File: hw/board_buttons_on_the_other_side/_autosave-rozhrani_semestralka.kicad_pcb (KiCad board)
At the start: 2 copper layers, 152 x 38.6 mm, 64 parts, among them P1 DISPLAY_CONN, P2 DISPLAY_VCC_CON, P3 USB_B, U1 MCP2210, U2 MIC5504-3.3, U3 Joystick, U4 LM239, U5 CD4532, U6 NPIC6C596, U7 NE555, U8 PB6149L, U9 PB6149L

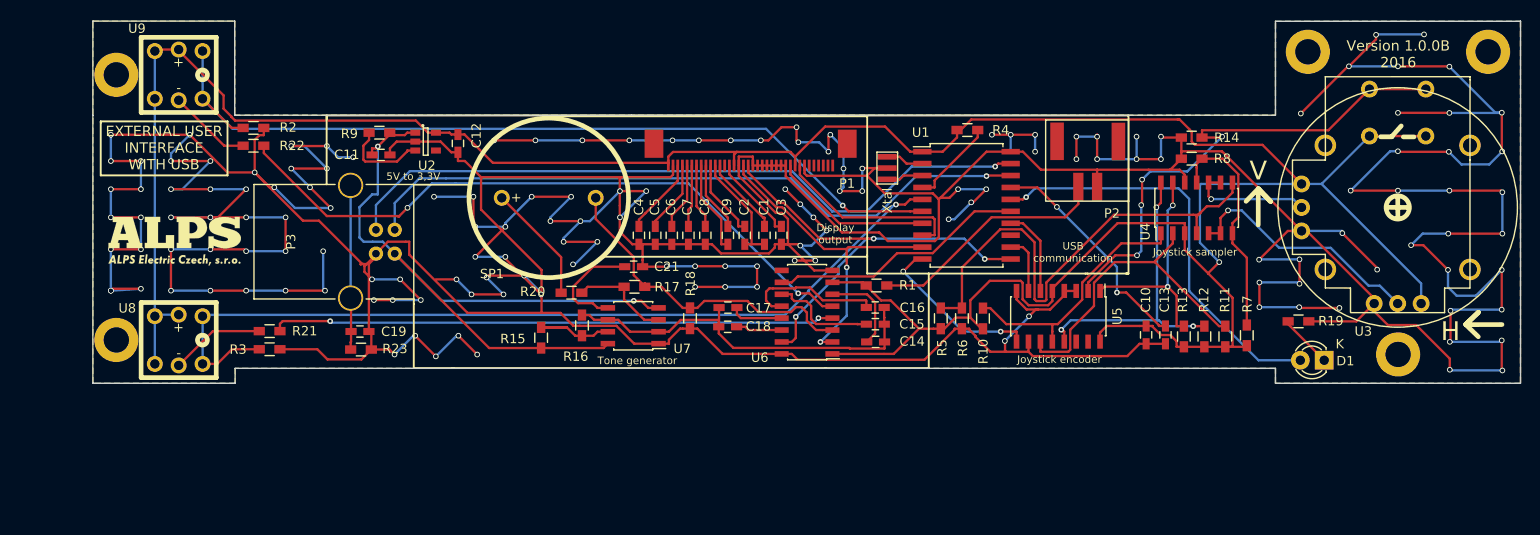
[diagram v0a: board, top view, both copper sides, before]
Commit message: Aladin v 1.2.0 pcb - repaired GPIO for /CE and also BUZZERs capacitors, some footprints had change
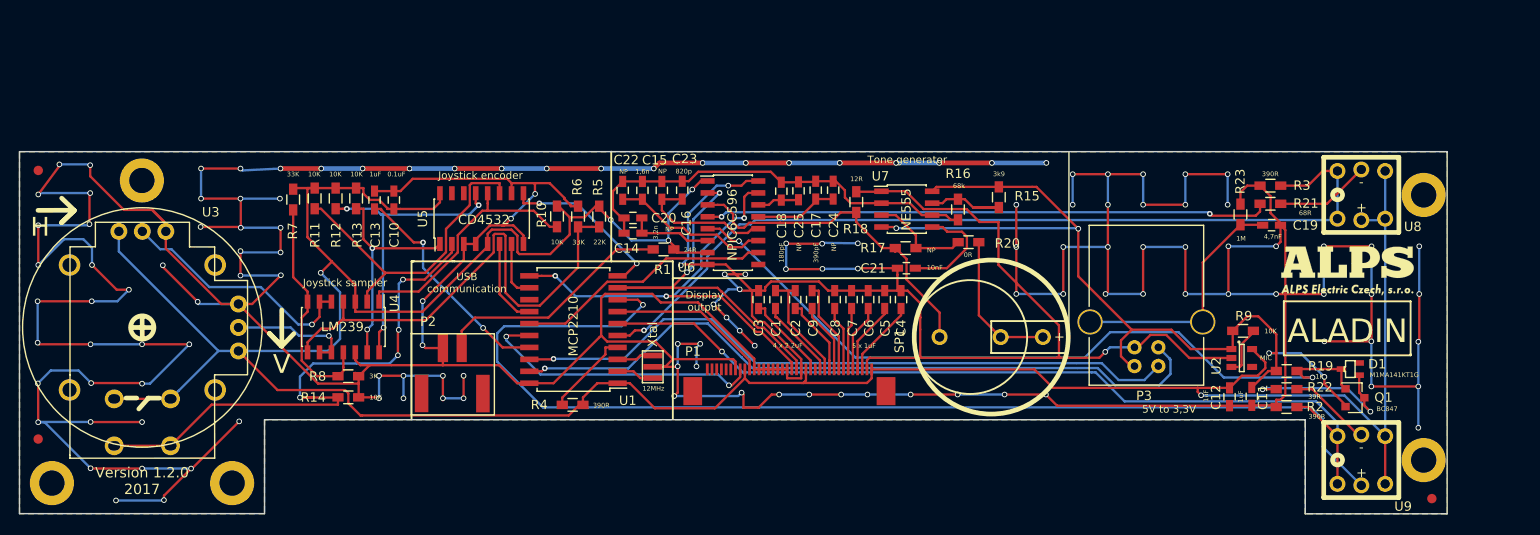
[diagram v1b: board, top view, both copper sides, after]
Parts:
- added C20: NP, Capacitors_SMD:C_0603_HandSoldering, F.Cu at (132.2, 103.7)
- added C22: NP, Capacitors_SMD:C_0603_HandSoldering, F.Cu at (131.1, 100.7)
- added C23: NP, Capacitors_SMD:C_0603_HandSoldering, F.Cu at (135.3, 100.7)
- added C24: NP, Capacitors_SMD:C_0603_HandSoldering, F.Cu at (153.5, 100.7)
- added C25: NP, Capacitors_SMD:C_0603_HandSoldering, F.Cu at (149.8, 100.8)
- added FID1: Fiducial_1mm_Dia_2.54mm_Outer_CopperTop, Fiducials:Fiducial_1mm_Dia_2.54mm_Outer_CopperTop, F.Cu at (68.9, 98.6)
- added FID2: Fiducial_1mm_Dia_2.54mm_Outer_CopperTop, Fiducials:Fiducial_1mm_Dia_2.54mm_Outer_CopperTop, F.Cu at (68.9, 127.2)
- added FID3**: Fiducial_1mm_Dia_2.54mm_Outer_CopperTop, Fiducials:Fiducial_1mm_Dia_2.54mm_Outer_CopperTop, F.Cu at (217.2, 133.5)
- added Q1: BC847, TO_SOT_Packages_SMD:SOT-23, F.Cu at (209.1, 122.8)
- C14: value 0 -> 3,2n
- C15: value 0 -> 1,6n
- C16: value 0 -> 820p
- C17: value 0 -> 390pF
- C18: value 0 -> 180pF
- D1: value L-1334SRT -> M1MA141KT1G; footprint LEDs:LED-3MM -> TO_SOT_Packages_SMD:SOT-323
- R1: value 24 -> 24R
- R17: value 10K -> NP
- R18: value 10K -> 12R
- R19: value 390R -> 1K
- R2, R3, R4: value 390 -> 390R
- R21: value 68 -> 68R
- R22: value 68 -> 39R
- U2: value MIC5504-3.3 -> MIC
- U9: value PB6149L -> PB6149Ldual
- moved REF** 159.7 mm to (70.3, 131.9), turned to 180 degrees
- moved REF** 145.1 mm to (216.4, 129.4), turned to 180 degrees
- moved REF** 140.0 mm to (216.4, 101.2), turned to 180 degrees
- moved REF** 135.0 mm to (79.9, 99.7), turned to 180 degrees
- moved U3 134.3 mm to (80.0, 115.3), turned to 180 degrees
- moved U9 132.4 mm to (209.7, 129.4), turned to 180 degrees
- moved U8 126.9 mm to (209.7, 101.2), turned to 180 degrees
- moved G*** 124.9 mm to (208.3, 109.3)
- moved REF** 123.4 mm to (89.5, 131.9), turned to 180 degrees
- moved R2 113.9 mm to (201.8, 123.8), turned to 0 degrees
- moved R22 113.0 mm to (201.8, 121.9), turned to 0 degrees
- moved R3 108.0 mm to (200.1, 100.2), turned to 180 degrees
- moved R21 107.4 mm to (200.1, 102.2), turned to 180 degrees
- moved R7 102.6 mm to (96.0, 101.7), turned to 90 degrees
- moved R11 98.1 mm to (98.3, 101.6), turned to 90 degrees
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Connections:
- D1 pad 1: Net-(D1-Pad1) -> /BUT_LED
- D1 pad 2: /SIGNAL_LED -> Net-(D1-Pad2)
- R19 pad 1: GND -> /REG2
- R19 pad 2: Net-(D1-Pad1) -> VCC
- R22 pad 1: /REG2 -> /BUT_LED
- U1 pad 16: /SIGNAL_LED -> //CE
- U1 pad 8: //CE -> /SIGNAL_LED
- U9 pad 3: +3V3 -> /SIGNAL_LED
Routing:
- net /SIGNAL_LED: track 44.7 -> 122.0 mm
- net GND: track 966.4 -> 944.1 mm, vias 153 -> 137
- net /BUT_LED: track 0.00 -> 18.4 mm, vias 0 -> 2
- net VCC: track 79.1 -> 95.7 mm, vias 2 -> 4
- net //CE: track 20.3 -> 31.6 mm, vias 0 -> 2
- net /REG2: track 71.1 -> 82.2 mm
- net Net-(C19-Pad1): track 17.5 -> 26.4 mm
- net (no net): track 8.20 -> 0.00 mm, vias 4 -> 0
- net /MOSI: track 35.7 -> 42.5 mm
- net /JOY_C: track 54.6 -> 61.3 mm
- net Net-(D1-Pad1): track 6.30 -> 0.00 mm
- net +3V3: track 325.5 -> 331.8 mm, vias 1 -> 5
- net /REG4: track 11.4 -> 16.9 mm
- net Net-(R9-Pad2): track 9.27 -> 5.34 mm
- net Net-(C14-Pad1): track 42.0 -> 45.4 mm
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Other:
- outline, holes or cut-outs redrawn
- board text added: "4 x 2.2uF"
- board text added: "5 x 1uF"
- board text added: "ALADIN"
- board text added: "Version 1.2.0 2017"
- board text removed: "EXTERNAL USER INTERFACE WITH USB"
- board text removed: "Version 1.0.0B 2016"
